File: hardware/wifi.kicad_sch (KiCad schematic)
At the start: 0 parts

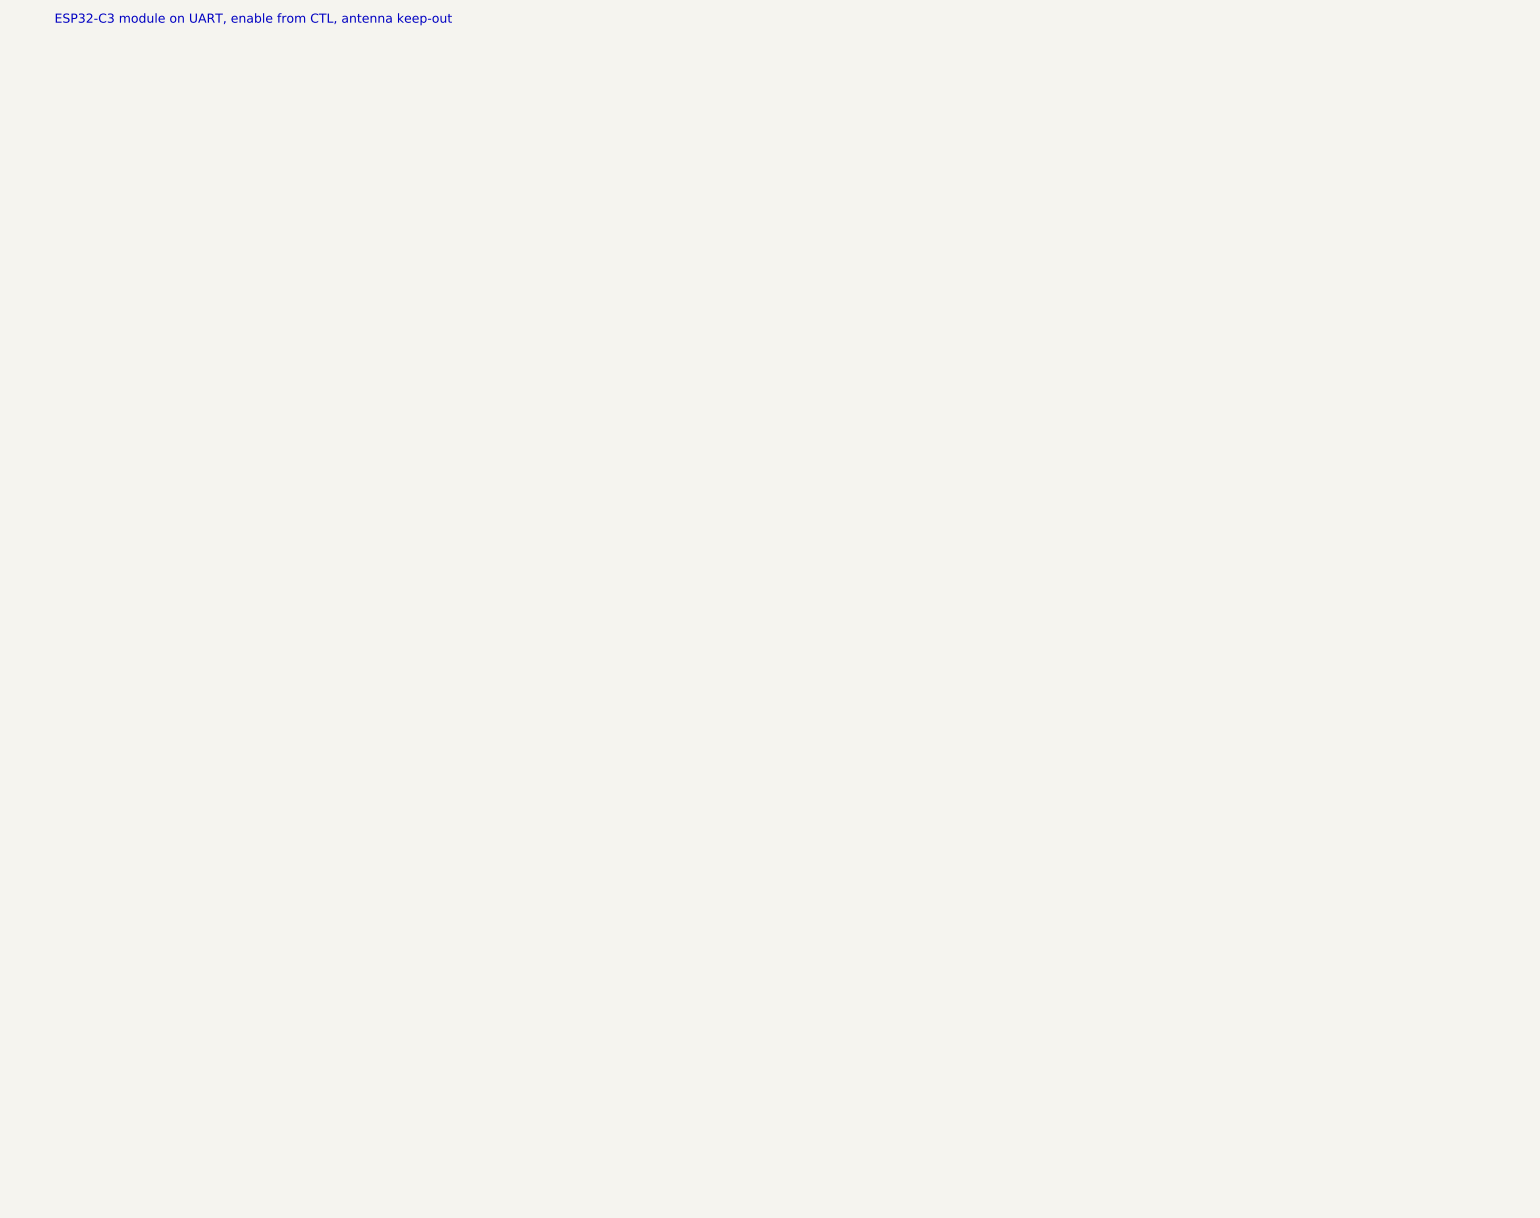
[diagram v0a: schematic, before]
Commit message: Remaining sheets: power, SD and display, WiFi, audio, joystick; ERC clean
- Power: Schottky diode-OR of edge +5V and USB VBUS (card runs from the
  2068/expansion bus, USB alone, or both), two TLV1117LV33 LDOs, bulk caps
- SD: Hirose DM3AT in SPI mode with series R, pull-ups, card detect to STAT
- OLED: 7-pin header (Waveshare 1.27in 128x96 SSD1351) on SPI1
- WiFi: ESP32-C3-WROOM-02 on UART, EN/boot from CTL, IO8 pull-up
- Audio: PWM low-pass, 2068 SOUND mix, MCP6002 buffers, 3.5 mm jack
- Joystick: DE-9 Kempston with pull-ups, series R, optional +5V jumper
- Memory sheet: activity LED on CTL bit 6
- Docs: power decision updated

Co-Authored-By: Claude Fable 5.1 <noreply@anthropic.com>
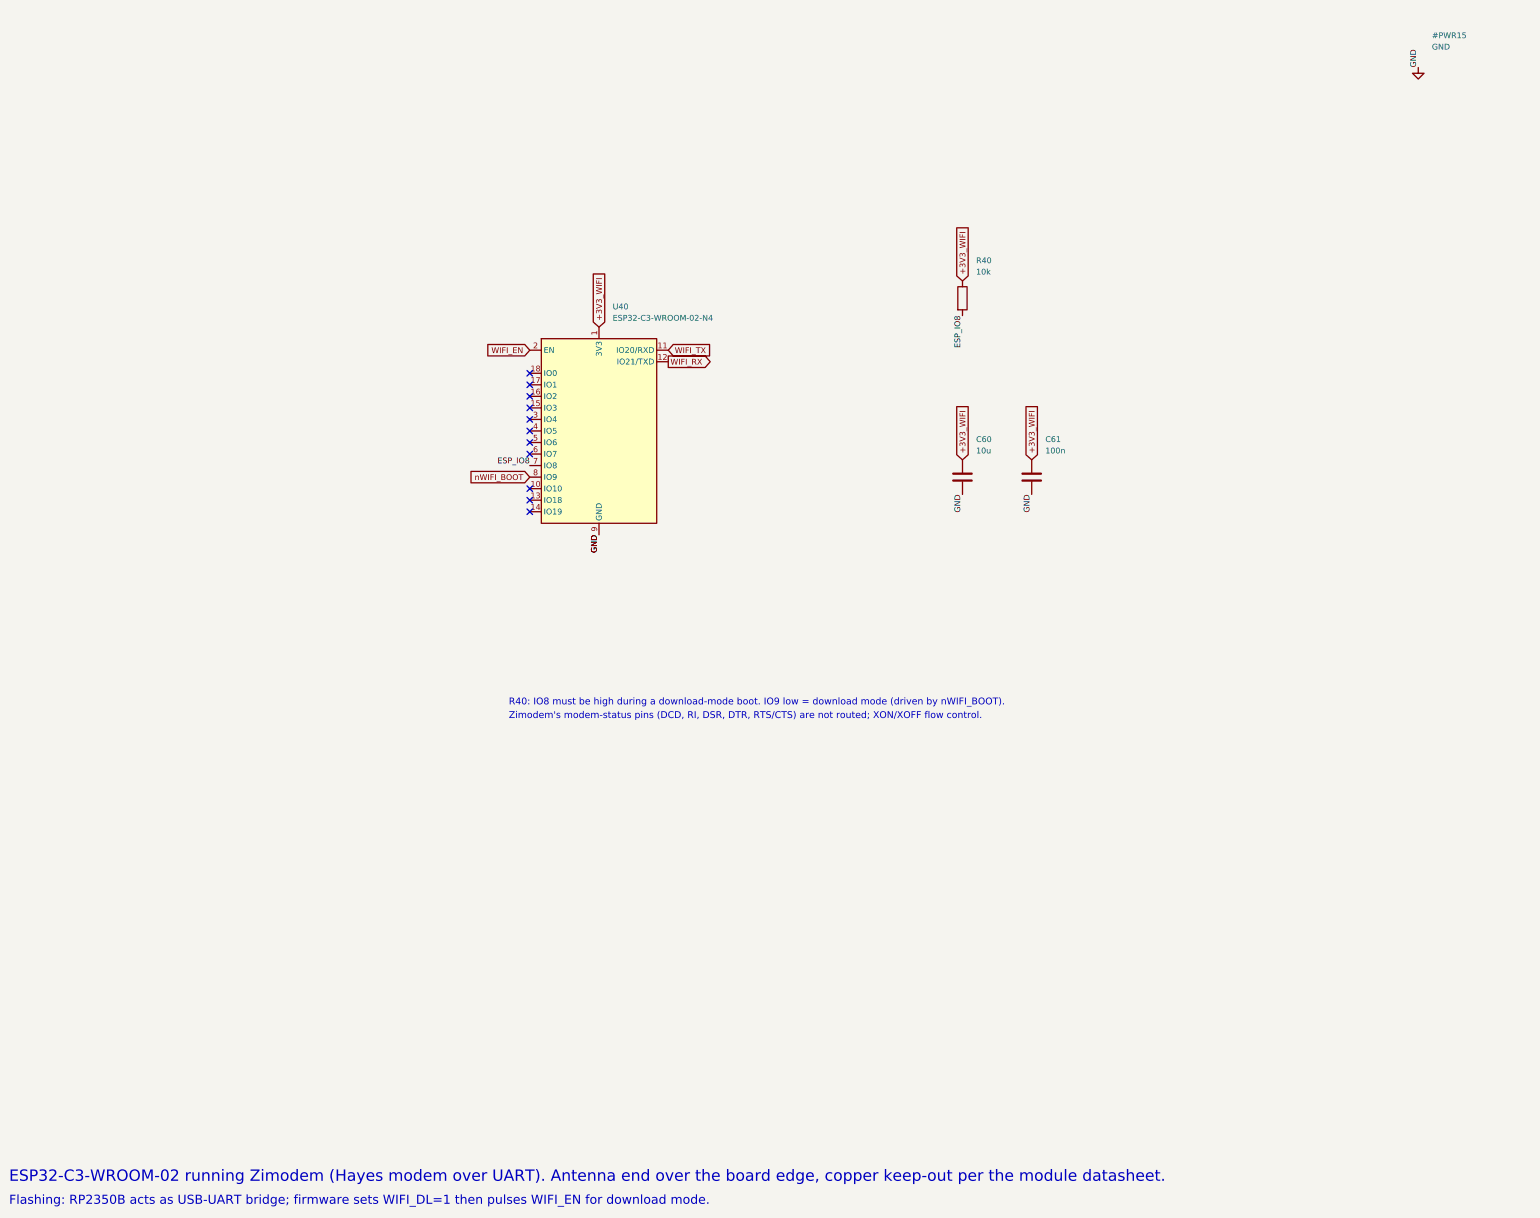
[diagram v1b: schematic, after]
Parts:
- added C60: 10u, Capacitor_SMD:C_0805_2012Metric, symbol Device:C
- added C61: 100n, Capacitor_SMD:C_0603_1608Metric, symbol Device:C
- added R40: 10k, Resistor_SMD:R_0603_1608Metric, symbol Device:R
- added U40: ESP32-C3-WROOM-02-N4, RF_Module:ESP32-C3-WROOM-02, symbol RF_Module:ESP32-C3-WROOM-02
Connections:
- new net +3V3_WIFI: C60.1, C61.1, R40.1, U40.1 (3V3)
- new net ESP_IO8: R40.2, U40.7 (IO8)
- new net GND: C60.2, C61.2, U40.19 (GND), U40.9 (GND)
- new net WIFI_EN: U40.2 (EN)
- new net WIFI_RX: U40.12 (IO21/TXD)
- new net WIFI_TX: U40.11 (IO20/RXD)
- new net nWIFI_BOOT: U40.8 (IO9)
- no-connect marks 0 -> 11
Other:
- note added: "ESP32-C3-WROOM-02 running Zimodem (Hayes modem over UART). Antenna end over the board edge, copper keep-out per the module datasheet."
- note added: "Flashing: RP2350B acts as USB-UART bridge; firmware sets WIFI_DL=1 then pulses WIFI_EN for download mode."
- note added: "R40: IO8 must be high during a download-mode boot. IO9 low = download mode (driven by nWIFI_BOOT)."
- note added: "Zimodem's modem-status pins (DCD, RI, DSR, DTR, RTS/CTS) are not routed; XON/XOFF flow control."
- note removed: "ESP32-C3 module on UART, enable from CTL, antenna keep-out"
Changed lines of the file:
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@@
-(kicad_sch (version 20250114) (generator "gen_board.py") (generator_version "1")
+(kicad_sch (version 20250114) (generator "schlib.py") (generator_version "1")
   (paper "A3")
   (title_block (title "TS-Pico v3: WiFi") (rev "0.1") (company "Timex/Sinclair Online User Group"))
-  (text "ESP32-C3 module on UART, enable from CTL, antenna keep-out" (exclude_from_sim no) (at 30 30 0) (effects (font (size 2 2)) (justify left bottom)))
+  (text "ESP32-C3-WROOM-02 running Zimodem (Hayes modem over UART). Antenna end over the board edge, copper keep-out per the module datasheet." (exclude_from_sim no) (at 20 285 0) (effects (font (size 2.5 2.5)) (justify left bottom)))
+  (text "Flashing: RP2350B acts as USB-UART bridge; firmware sets WIFI_DL=1 then pulses WIFI_EN for download mode." (exclude_from_sim no) (at 20 290 0) (effects (font (size 2.0 2.0)) (justify left bottom)))
+  (symbol (lib_id "power:GND") (at 330.2 39.37 0) (unit 1)
+    (exclude_from_sim no) (in_bom yes) (on_board yes) (dnp no)
+    (property "Reference" "#PWR15" (at 333.2 32.33 0) (effects (font (size 1.27 1.27)) (justify left)))
+    (property "Value" "GND" (at 333.2 34.83 0) (effects (font (size 1.27 1.27)) (justify left)))
+    (property "Footprint" "" (at 330.2 39.37 0) (effects (font (size 1.27 1.27)) (justify left) (hide yes)))
+    (property "Datasheet" "" (at 330.2 39.37 0) (effects (font (size 1.27 1.27)) (justify left) (hide yes)))
+    (property "Description" "" (at 330.2 39.37 0) (effects (font (size 1.27 1.27)) (justify left) (hide yes)))
+    (pin "1")
+    (instances (project "tspico-v3" (path "/9088d141-8624-4d5c-91a9-7a3a7a90b3cc/d28d46ae-5d37-4c4f-b909-43ed531db596" (reference "#PWR15") (unit 1))))
+  )
+  (label "GND" (at 330.20 39.37 90) (effects (font (size 1.27 1.27)) (justify left bottom)))
+  (symbol (lib_id "RF_Module:ESP32-C3-WROOM-02") (at 149.86 119.38 0) (unit 1)
+    (exclude_from_sim no) (in_bom yes) (on_board yes) (dnp no)
+    (property "Reference" "U40" (at 152.86 92.02 0) (effects (font (size 1.27 1.27)) (justify left)))
+    (property "Value" "ESP32-C3-WROOM-02-N4" (at 152.86 94.52 0) (effects (font (size 1.27 1.27)) (justify left)))
+    (property "Footprint" "RF_Module:ESP32-C3-WROOM-02" (at 149.86 119.38 0) (effects (font (size 1.27 1.27)) (justify left) (hide yes)))
+    (property "Datasheet" "" (at 149.86 119.38 0) (effects (font (size 1.27 1.27)) (justify left) (hide yes)))
+    (property "Description" "" (at 149.86 119.38 0) (effects (font (size 1.27 1.27)) (justify left) (hide yes)))
+    (pin "1")
+    (pin "2")
+    (pin "3")
+    (pin "4")
+    (pin "5")
+    (pin "6")
+    (pin "7")
+    (pin "8")
+    (pin "9")
+    (pin "10")
+    (pin "11")
+    (pin "12")
+    (pin "13")
+    (pin "14")
+    (pin "15")
+    (pin "16")
+    (pin "17")
+    (pin "18")
+    (pin "19")
+    (instances (project "tspico-v3" (path "/9088d141-8624-4d5c-91a9-7a3a7a90b3cc/d28d46ae-5d37-4c4f-b909-43ed531db596" (reference "U40") (unit 1))))
+  )
+  (global_label "+3V3_WIFI" (shape input) (at 149.86 96.52 90) (effects (font (size 1.27 1.27)) (justify left)))
+  (label "GND" (at 149.86 142.24 270) (effects (font (size 1.27 1.27)) (justify right bottom)))
+  (label "GND" (at 149.86 142.24 270) (effects (font (size 1.27 1.27)) (justify right bottom)))
+  (global_label "WIFI_EN" (shape input) (at 134.62 101.60 180) (effects (font (size 1.27 1.27)) (justify right)))
+  (global_label "nWIFI_BOOT" (shape input) (at 134.62 129.54 180) (effects (font (size 1.27 1.27)) (justify right)))
+  (label "ESP_IO8" (at 134.62 127.00 180) (effects (font (size 1.27 1.27)) (justify right bottom)))
+  (global_label "WIFI_TX" (shape input) (at 165.10 101.60 0) (effects (font (size 1.27 1.27)) (justify left)))
+  (global_label "WIFI_RX" (shape output) (at 165.10 104.14 0) (effects (font (size 1.27 1.27)) (justify left)))
+  (no_connect (at 134.62 116.84))
+  (no_connect (at 134.62 119.38))
+  (no_connect (at 134.62 121.92))
+  (no_connect (at 134.62 124.46))
+  (no_connect (at 134.62 132.08))
+  (no_connect (at 134.62 134.62))
+  (no_connect (at 134.62 137.16))
+  (no_connect (at 134.62 114.30))
+  (no_connect (at 134.62 111.76))
+  (no_connect (at 134.62 109.22))
+  (no_connect (at 134.62 106.68))
+  (symbol (lib_id "Device:R") (at 229.87 90.17 0) (unit 1)
+    (exclude_from_sim no) (in_bom yes) (on_board yes) (dnp no)
+    (property "Reference" "R40" (at 232.87 81.86 0) (effects (font (size 1.27 1.27)) (justify left)))
+    (property "Value" "10k" (at 232.87 84.36 0) (effects (font (size 1.27 1.27)) (justify left)))
+    (property "Footprint" "Resistor_SMD:R_0603_1608Metric" (at 229.87 90.17 0) (effects (font (size 1.27 1.27)) (justify left) (hide yes)))
+    (property "Datasheet" "" (at 229.87 90.17 0) (effects (font (size 1.27 1.27)) (justify left) (hide yes)))
+    (property "Description" "" (at 229.87 90.17 0) (effects (font (size 1.27 1.27)) (justify left) (hide yes)))
+    (pin "1")
+    (pin "2")
+    (instances (project "tspico-v3" (path "/9088d141-8624-4d5c-91a9-7a3a7a90b3cc/d28d46ae-5d37-4c4f-b909-43ed531db596" (reference "R40") (unit 1))))
+  )
+  (global_label "+3V3_WIFI" (shape input) (at 229.87 86.36 90) (effects (font (size 1.27 1.27)) (justify left)))
+  (label "ESP_IO8" (at 229.87 93.98 270) (effects (font (size 1.27 1.27)) (justify right bottom)))
+  (symbol (lib_id "Device:C") (at 229.87 129.54 0) (unit 1)
+    (exclude_from_sim no) (in_bom yes) (on_board yes) (dnp no)
+    (property "Reference" "C60" (at 232.87 121.23 0) (effects (font (size 1.27 1.27)) (justify left)))
+    (property "Value" "10u" (at 232.87 123.73 0) (effects (font (size 1.27 1.27)) (justify left)))
+    (property "Footprint" "Capacitor_SMD:C_0805_2012Metric" (at 229.87 129.54 0) (effects (font (size 1.27 1.27)) (justify left) (hide yes)))
+    (property "Datasheet" "" (at 229.87 129.54 0) (effects (font (size 1.27 1.27)) (justify left) (hide yes)))
+    (property "Description" "" (at 229.87 129.54 0) (effects (font (size 1.27 1.27)) (justify left) (hide yes)))
+    (pin "1")
+    (pin "2")
+    (instances (project "tspico-v3" (path "/9088d141-8624-4d5c-91a9-7a3a7a90b3cc/d28d46ae-5d37-4c4f-b909-43ed531db596" (reference "C60") (unit 1))))
+  )
+  (global_label "+3V3_WIFI" (shape input) (at 229.87 125.73 90) (effects (font (size 1.27 1.27)) (justify left)))
+  (label "GND" (at 229.87 133.35 270) (effects (font (size 1.27 1.27)) (justify right bottom)))
+  (symbol (lib_id "Device:C") (at 245.11 129.54 0) (unit 1)
+    (exclude_from_sim no) (in_bom yes) (on_board yes) (dnp no)
+    (property "Reference" "C61" (at 248.11 121.23 0) (effects (font (size 1.27 1.27)) (justify left)))
+    (property "Value" "100n" (at 248.11 123.73 0) (effects (font (size 1.27 1.27)) (justify left)))
+    (property "Footprint" "Capacitor_SMD:C_0603_1608Metric" (at 245.11 129.54 0) (effects (font (size 1.27 1.27)) (justify left) (hide yes)))
+    (property "Datasheet" "" (at 245.11 129.54 0) (effects (font (size 1.27 1.27)) (justify left) (hide yes)))
+    (property "Description" "" (at 245.11 129.54 0) (effects (font (size 1.27 1.27)) (justify left) (hide yes)))
+    (pin "1")
+    (pin "2")
+    (instances (project "tspico-v3" (path "/9088d141-8624-4d5c-91a9-7a3a7a90b3cc/d28d46ae-5d37-4c4f-b909-43ed531db596" (reference "C61") (unit 1))))
+  )
+  (global_label "+3V3_WIFI" (shape input) (at 245.11 125.73 90) (effects (font (size 1.27 1.27)) (justify left)))
+  (label "GND" (at 245.11 133.35 270) (effects (font (size 1.27 1.27)) (justify right bottom)))
+  (text "R40: IO8 must be high during a download-mode boot. IO9 low = download mode (driven by nWIFI_BOOT)." (exclude_from_sim no) (at 130 180 0) (effects (font (size 1.5 1.5)) (justify left bottom)))
+  (text "Zimodem's modem-status pins (DCD, RI, DSR, DTR, RTS/CTS) are not routed; XON/XOFF flow control." (exclude_from_sim no) (at 130 183 0) (effects (font (size 1.5 1.5)) (justify left bottom)))
   (embedded_fonts no)
 )

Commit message: BOM pass: LCSC and MPN fields on every part, JLCPCB BOM export
- scripts/parts.py: part table looked up 2026-09-16; schlib stamps fields
- substitutions for stock: 74HC273PW, 74LVC139PW, TI LVC04/08/126/574/1G86,
  33R USB series, XKB TS-1187A switches, Panasonic polymer 220uF, B5819W
- bom/: JLCPCB-format and full BOM CSVs

Co-Authored-By: Claude Fable 5.1 <noreply@anthropic.com>
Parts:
- C60: LCSC (none) -> C15850; MPN (none) -> CL21A106KAYNNNE
- C61: LCSC (none) -> C14663; MPN (none) -> CC0603KRX7R9BB104
- R40: LCSC (none) -> C25804; MPN (none) -> 0603WAF1002T5E
- U40: LCSC (none) -> C2934560; MPN (none) -> ESP32-C3-WROOM-02-N4
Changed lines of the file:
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@@
     (property "Datasheet" "" (at 149.86 119.38 0) (effects (font (size 1.27 1.27)) (justify left) (hide yes)))
     (property "Description" "" (at 149.86 119.38 0) (effects (font (size 1.27 1.27)) (justify left) (hide yes)))
+    (property "MPN" "ESP32-C3-WROOM-02-N4" (at 149.86 119.38 0) (effects (font (size 1.27 1.27)) (justify left) (hide yes)))
+    (property "LCSC" "C2934560" (at 149.86 119.38 0) (effects (font (size 1.27 1.27)) (justify left) (hide yes)))
     (pin "1")
     (pin "2")
@@
     (property "Datasheet" "" (at 229.87 90.17 0) (effects (font (size 1.27 1.27)) (justify left) (hide yes)))
     (property "Description" "" (at 229.87 90.17 0) (effects (font (size 1.27 1.27)) (justify left) (hide yes)))
+    (property "MPN" "0603WAF1002T5E" (at 229.87 90.17 0) (effects (font (size 1.27 1.27)) (justify left) (hide yes)))
+    (property "LCSC" "C25804" (at 229.87 90.17 0) (effects (font (size 1.27 1.27)) (justify left) (hide yes)))
     (pin "1")
     (pin "2")
@@
     (property "Datasheet" "" (at 229.87 129.54 0) (effects (font (size 1.27 1.27)) (justify left) (hide yes)))
     (property "Description" "" (at 229.87 129.54 0) (effects (font (size 1.27 1.27)) (justify left) (hide yes)))
+    (property "MPN" "CL21A106KAYNNNE" (at 229.87 129.54 0) (effects (font (size 1.27 1.27)) (justify left) (hide yes)))
+    (property "LCSC" "C15850" (at 229.87 129.54 0) (effects (font (size 1.27 1.27)) (justify left) (hide yes)))
     (pin "1")
     (pin "2")
@@
     (property "Datasheet" "" (at 245.11 129.54 0) (effects (font (size 1.27 1.27)) (justify left) (hide yes)))
     (property "Description" "" (at 245.11 129.54 0) (effects (font (size 1.27 1.27)) (justify left) (hide yes)))
+    (property "MPN" "CC0603KRX7R9BB104" (at 245.11 129.54 0) (effects (font (size 1.27 1.27)) (justify left) (hide yes)))
+    (property "LCSC" "C14663" (at 245.11 129.54 0) (effects (font (size 1.27 1.27)) (justify left) (hide yes)))
     (pin "1")
     (pin "2")

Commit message: BOM cost optimisation against the JLCPCB catalog; schematic-side regulator fix
jlc_price.py prices the BOM via JLCPCB's parts API. Substitutions cut parts+fees
per board from $32.95 to $17.19 on a 10-board run: PSRAM DNP, electrolytic bulk
caps, TF-01A socket, PJ-320D jack, 74HC574, GD25Q128E, 0603 10 uF, basic LED,
preferred MCP6002; U16 decoder deleted (strobes on GPIO), U8 and U15 become
74LVC245s; J3/J5 hand-soldered. Adds the AOTA inductor and VREG_AVDD filter.
PCB needs a relayout; fab/ is stale.

Co-Authored-By: Claude Fable 5.1 <noreply@anthropic.com>
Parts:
- C60: footprint Capacitor_SMD:C_0805_2012Metric -> Capacitor_SMD:C_0603_1608Metric; LCSC C15850 -> C19702; MPN CL21A106KAYNNNE -> CL10A106KP8NNNC
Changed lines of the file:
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@@
     (property "Reference" "C60" (at 232.87 121.23 0) (effects (font (size 1.27 1.27)) (justify left)))
     (property "Value" "10u" (at 232.87 123.73 0) (effects (font (size 1.27 1.27)) (justify left)))
-    (property "Footprint" "Capacitor_SMD:C_0805_2012Metric" (at 229.87 129.54 0) (effects (font (size 1.27 1.27)) (justify left) (hide yes)))
+    (property "Footprint" "Capacitor_SMD:C_0603_1608Metric" (at 229.87 129.54 0) (effects (font (size 1.27 1.27)) (justify left) (hide yes)))
     (property "Datasheet" "" (at 229.87 129.54 0) (effects (font (size 1.27 1.27)) (justify left) (hide yes)))
     (property "Description" "" (at 229.87 129.54 0) (effects (font (size 1.27 1.27)) (justify left) (hide yes)))
-    (property "MPN" "CL21A106KAYNNNE" (at 229.87 129.54 0) (effects (font (size 1.27 1.27)) (justify left) (hide yes)))
-    (property "LCSC" "C15850" (at 229.87 129.54 0) (effects (font (size 1.27 1.27)) (justify left) (hide yes)))
+    (property "MPN" "CL10A106KP8NNNC" (at 229.87 129.54 0) (effects (font (size 1.27 1.27)) (justify left) (hide yes)))
+    (property "LCSC" "C19702" (at 229.87 129.54 0) (effects (font (size 1.27 1.27)) (justify left) (hide yes)))
     (pin "1")
     (pin "2")
